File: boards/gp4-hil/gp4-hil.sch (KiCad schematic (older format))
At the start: 0 parts

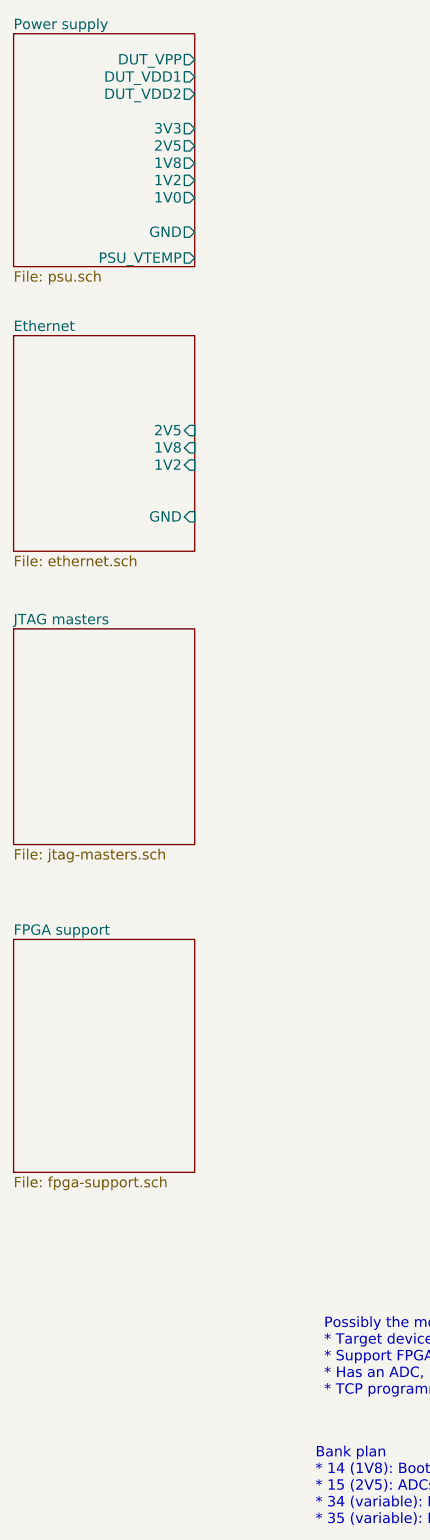
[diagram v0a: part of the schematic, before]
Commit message: Added load switches for DUT_VDDx rails
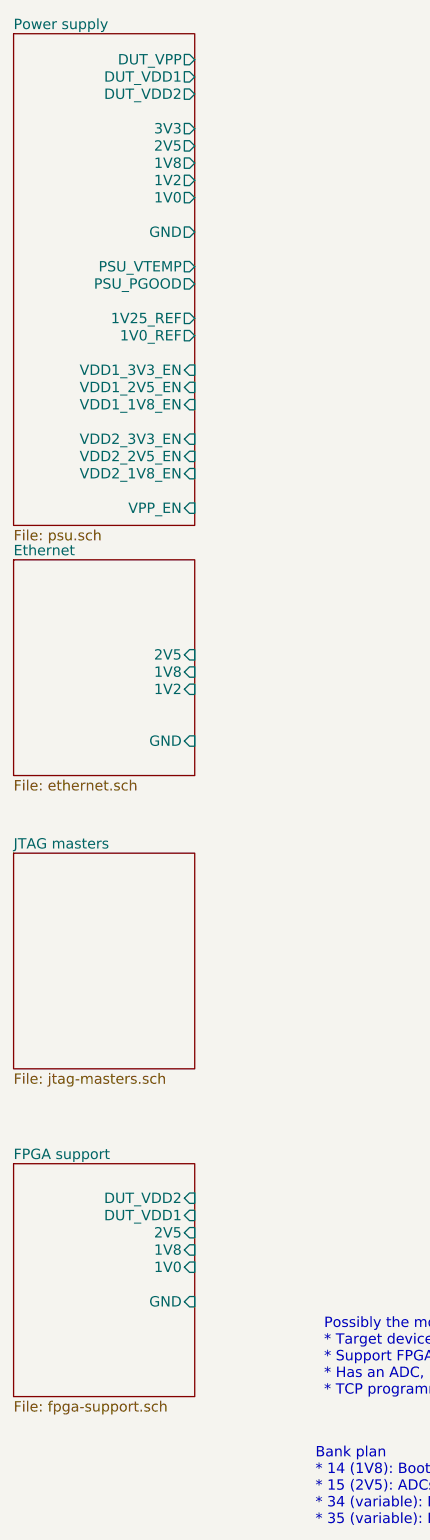
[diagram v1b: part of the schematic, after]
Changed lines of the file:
@@
 $EndDescr
 $Sheet
-S 1500 1200 1050 1350
+S 1500 1200 1050 2850
 U 57316A38
 F0 "Power supply" 60
@@
 F9 "DUT_VDD2" O R 2550 1550 60
 F10 "3V3" O R 2550 1750 60
-F11 "PSU_VTEMP" O R 2550 2500 60
+F11 "PSU_VTEMP" O R 2550 2550 60
+F12 "PSU_PGOOD" O R 2550 2650 60
+F13 "1V25_REF" O R 2550 2850 60
+F14 "1V0_REF" O R 2550 2950 60
+F15 "VDD1_3V3_EN" I R 2550 3150 60
+F16 "VDD1_1V8_EN" I R 2550 3350 60
+F17 "VDD1_2V5_EN" I R 2550 3250 60
+F18 "VDD2_3V3_EN" I R 2550 3550 60
+F19 "VDD2_1V8_EN" I R 2550 3750 60
+F20 "VDD2_2V5_EN" I R 2550 3650 60
+F21 "VPP_EN" I R 2550 3950 60
 $EndSheet
 $Sheet
-S 1500 2950 1050 1250
+S 1500 4250 1050 1250
 U 57316A40
 F0 "Ethernet" 60
 F1 "ethernet.sch" 60
-F2 "2V5" I R 2550 3500 60
-F3 "1V8" I R 2550 3600 60
-F4 "1V2" I R 2550 3700 60
-F5 "GND" I R 2550 4000 60
+F2 "2V5" I R 2550 4800 60
+F3 "1V8" I R 2550 4900 60
+F4 "1V2" I R 2550 5000 60
+F5 "GND" I R 2550 5300 60
 $EndSheet
 $Sheet
-S 1500 4650 1050 1250
+S 1500 5950 1050 1250
 U 57316A4B
 F0 "JTAG masters" 60
@@
 $EndSheet
 $Sheet
-S 1500 6450 1050 1350
+S 1500 7750 1050 1350
 U 57316B0C
 F0 "FPGA support" 60
 F1 "fpga-support.sch" 60
+F2 "GND" I R 2550 8550 60
+F3 "1V0" I R 2550 8350 60
+F4 "1V8" I R 2550 8250 60
+F5 "2V5" I R 2550 8150 60
+F6 "DUT_VDD1" I R 2550 8050 60
+F7 "DUT_VDD2" I R 2550 7950 60
 $EndSheet
 Text Notes 3250 9850 0    60   ~ 0

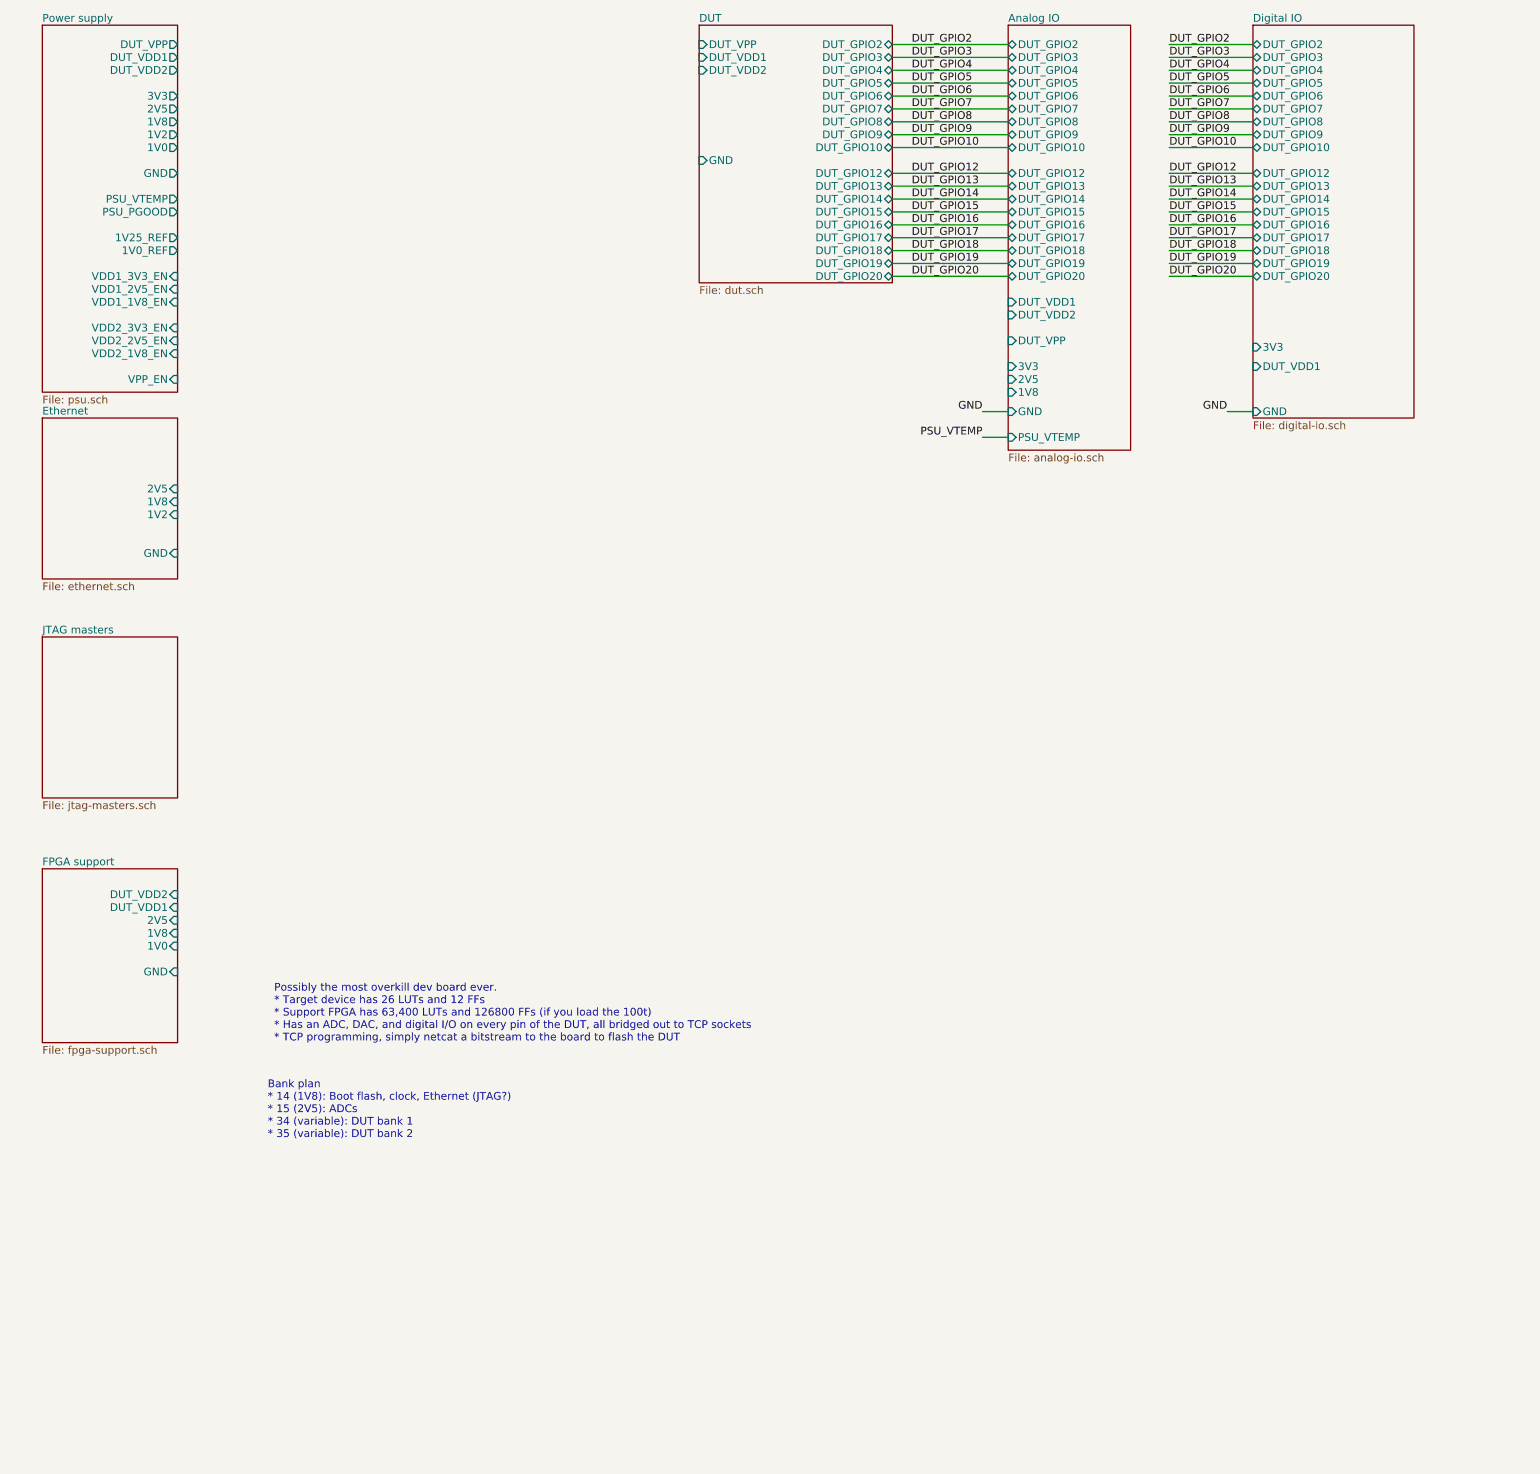
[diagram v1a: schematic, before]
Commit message: Merged JTAG master stuff with Ethernet schematic page
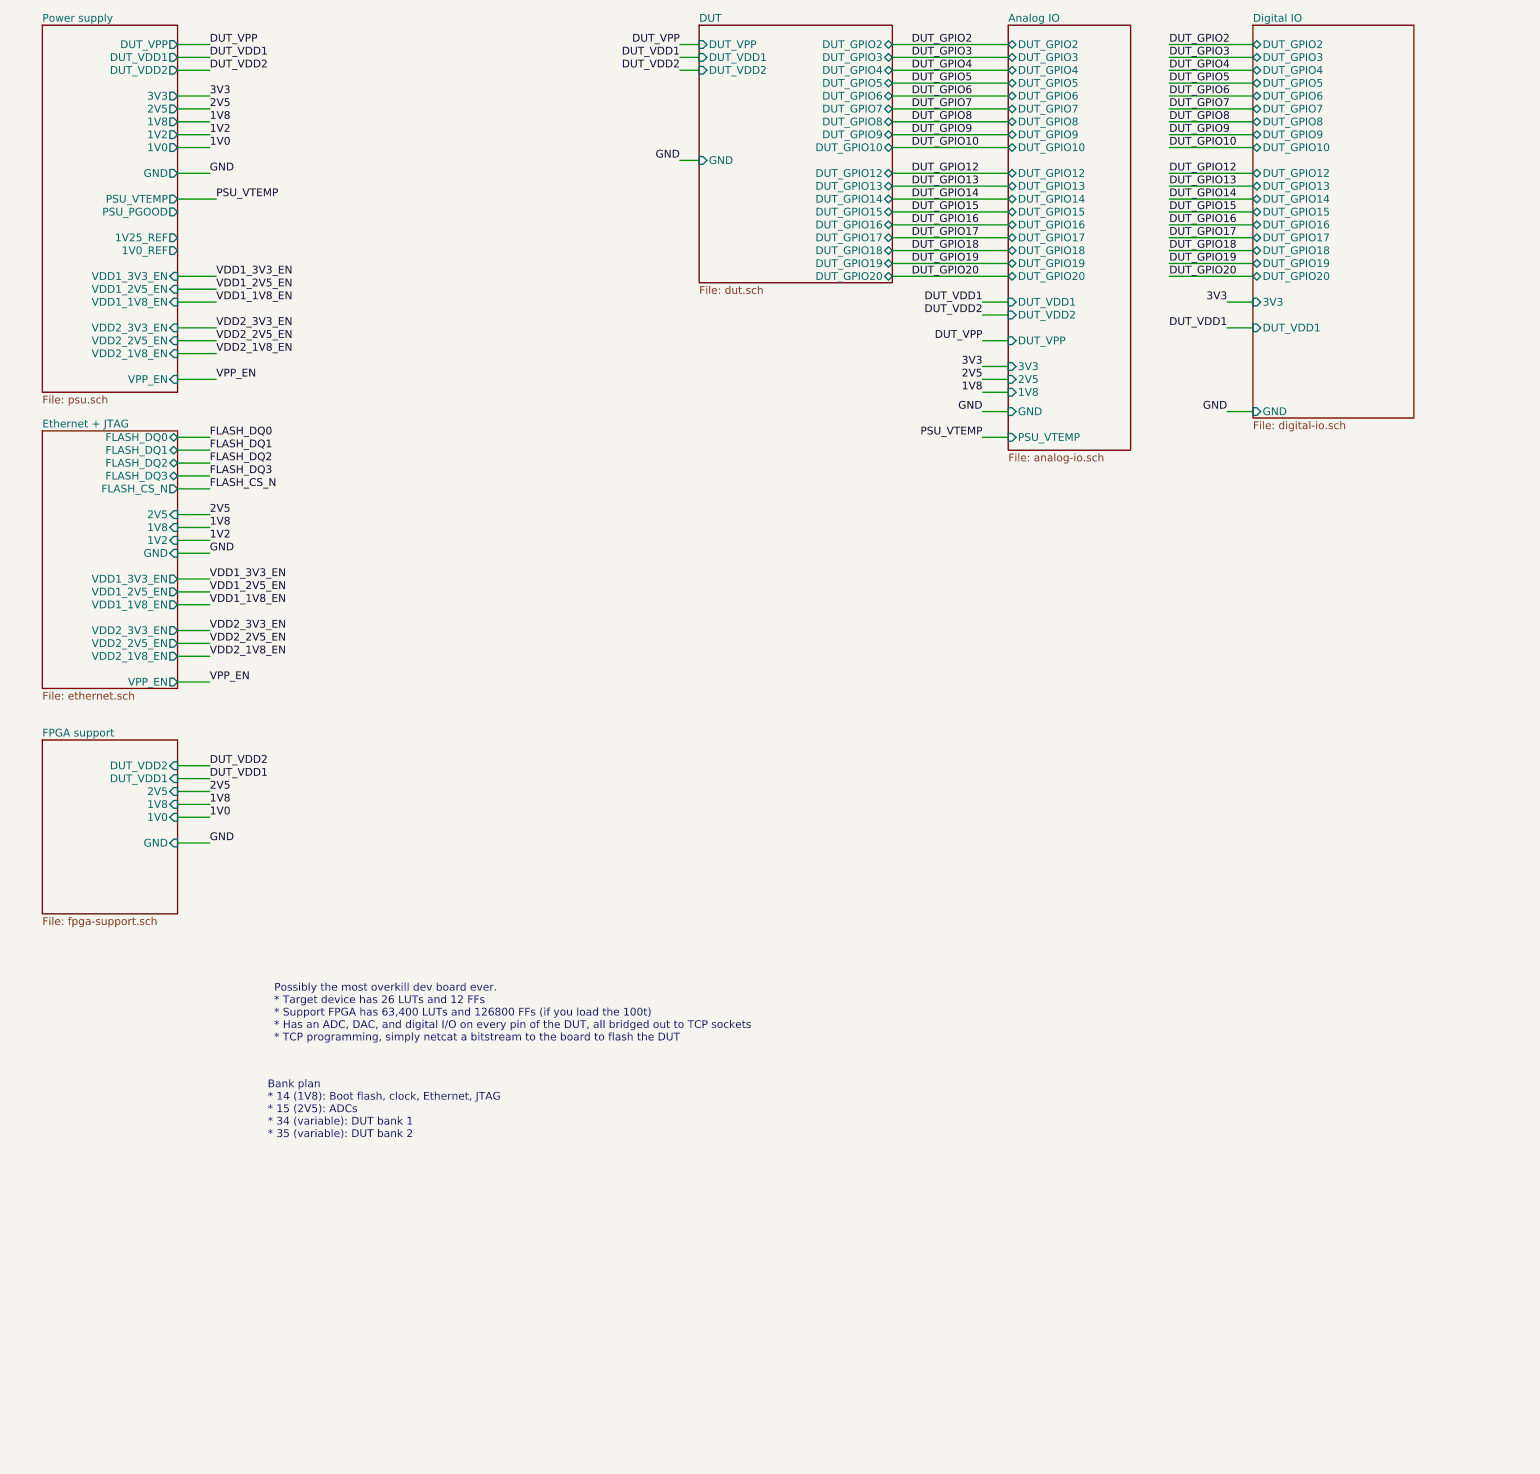
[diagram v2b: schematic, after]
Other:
- note added: "Bank plan\n* 14 (1V8): Boot flash, clock, Ethernet, JTAG\n* 15 (2V5): ADCs\n* 34 (variable): DUT bank 1\n* 35 (variable): DUT bank 2"
- note removed: "Bank plan\n* 14 (1V8): Boot flash, clock, Ethernet (JTAG?)\n* 15 (2V5): ADCs\n* 34 (variable): DUT bank 1\n* 35 (variable): DUT bank 2"

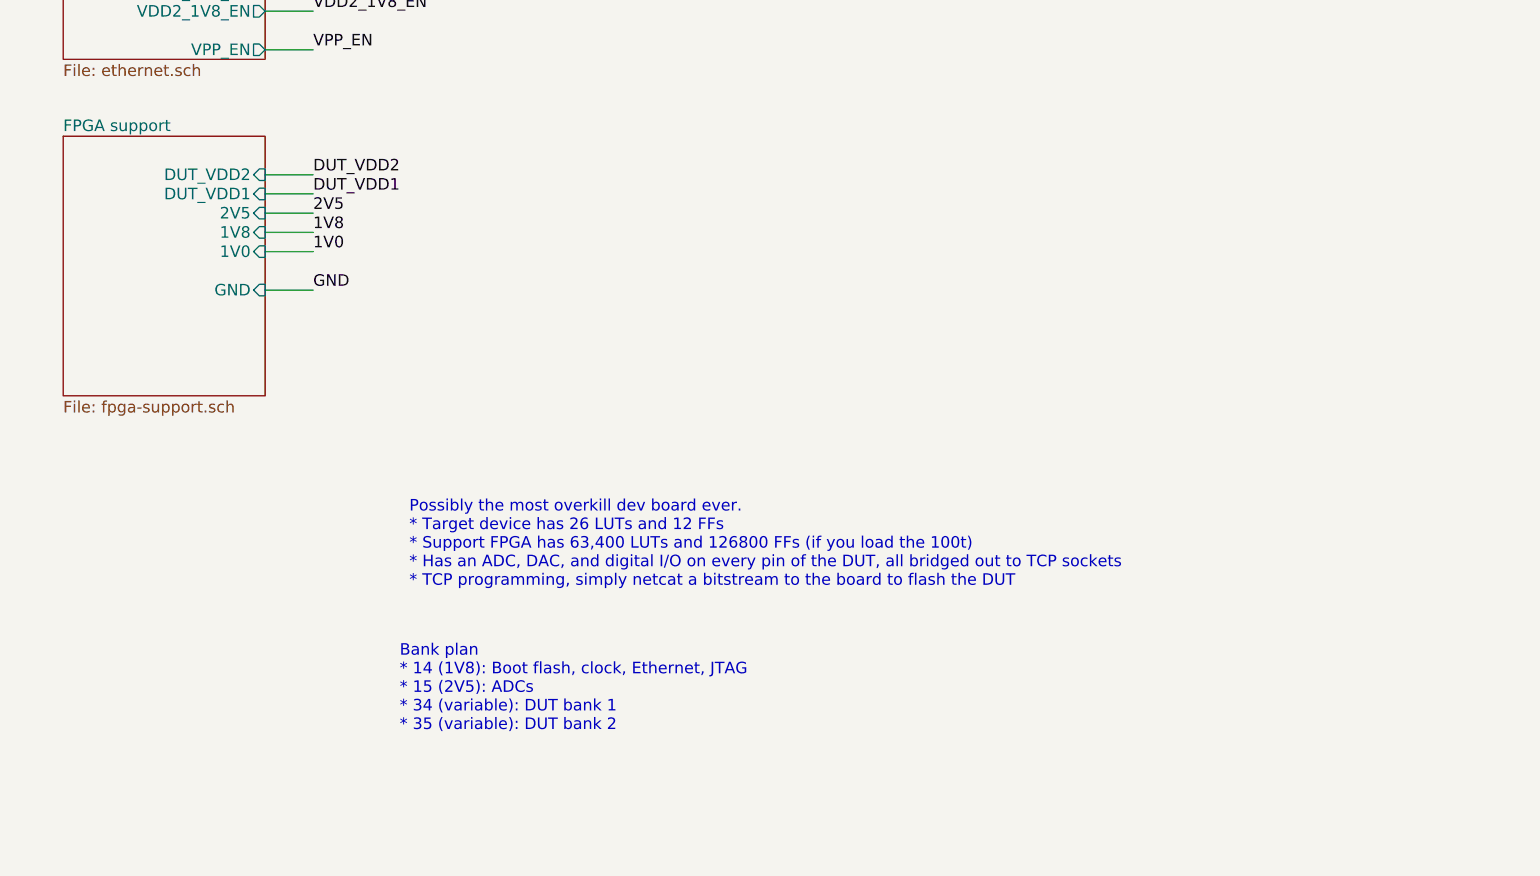
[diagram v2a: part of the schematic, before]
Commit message: Wired up FPGA config pins, flash, etc
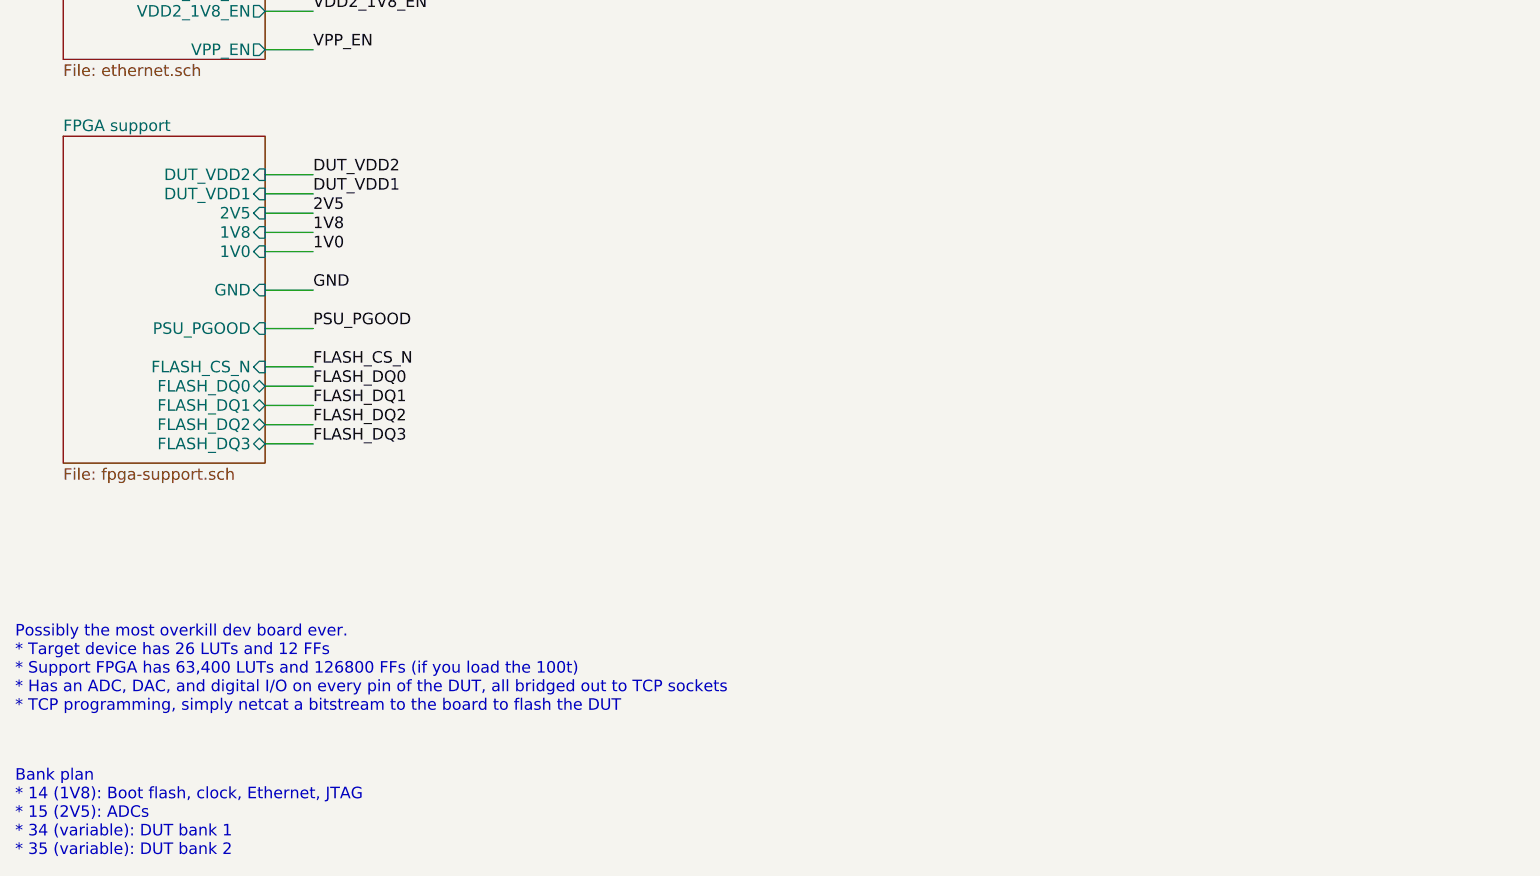
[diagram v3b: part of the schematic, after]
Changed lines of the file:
@@
 $EndSheet
 $Sheet
-S 1500 6750 1050 1350
+S 1500 6750 1050 1700
 U 57316B0C
 F0 "FPGA support" 60
@@
 F6 "DUT_VDD1" I R 2550 7050 60
 F7 "DUT_VDD2" I R 2550 6950 60
+F8 "PSU_PGOOD" I R 2550 7750 60
+F9 "FLASH_CS_N" I R 2550 7950 60
+F10 "FLASH_DQ0" B R 2550 8050 60
+F11 "FLASH_DQ1" B R 2550 8150 60
+F12 "FLASH_DQ2" B R 2550 8250 60
+F13 "FLASH_DQ3" B R 2550 8350 60
 $EndSheet
-Text Notes 3250 9850 0    60   ~ 0
+Text Notes 1250 10500 0    60   ~ 0
 Bank plan\n* 14 (1V8): Boot flash, clock, Ethernet, JTAG\n* 15 (2V5): ADCs\n* 34 (variable): DUT bank 1\n* 35 (variable): DUT bank 2
-Text Notes 3300 9100 0    60   ~ 0
+Text Notes 1250 9750 0    60   ~ 0
 Possibly the most overkill dev board ever.\n* Target device has 26 LUTs and 12 FFs\n* Support FPGA has 63,400 LUTs and 126800 FFs (if you load the 100t)\n* Has an ADC, DAC, and digital I/O on every pin of the DUT, all bridged out to TCP sockets\n* TCP programming, simply netcat a bitstream to the board to flash the DUT
 Text Label 8250 1350 0    60   ~ 0
@@
 Wire Wire Line
 	2800 7550 2550 7550
+Text Label 2800 7750 0    60   ~ 0
+PSU_PGOOD
+Wire Wire Line
+	2800 7750 2550 7750
+Text Label 2800 8050 0    60   ~ 0
+FLASH_DQ0
+Wire Wire Line
+	2800 7950 2550 7950
+Text Label 2800 8150 0    60   ~ 0
+FLASH_DQ1
+Wire Wire Line
+	2800 8050 2550 8050
+Text Label 2800 8250 0    60   ~ 0
+FLASH_DQ2
+Wire Wire Line
+	2800 8150 2550 8150
+Text Label 2800 8350 0    60   ~ 0
+FLASH_DQ3
+Wire Wire Line
+	2800 8250 2550 8250
+Text Label 2800 7950 0    60   ~ 0
+FLASH_CS_N
+Wire Wire Line
+	2800 8350 2550 8350
 $EndSCHEMATC
